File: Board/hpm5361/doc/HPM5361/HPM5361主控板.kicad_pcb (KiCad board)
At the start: 4 copper layers, 54.3 x 40 mm, 189 parts, among them J1 USB_C_Receptacle_USB2.0_16P, J2 Conn_02x05_Counter_Clockwise_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, J3 Conn_01x03_Pin, J4 Conn_01x02_Pin, J5 Conn_01x02_Pin, J7 Conn_01x02_Pin, Q1 AGM60P100A, Q2 PMBT3904, Q3 PMBT3904, Q4 AO3404A, U10 TJA1042TK-3, U11 TJA1042TK-3, U12 TJA1042TK-3, U13 RY8411, U14 LMR51450, U3 HPM5361ICB1, U5 USBLC6-2SC6, U6 W25Q128JVS, U7 SN65HVD75DRBR, U8 ICM-42688P-HXY, U9 TJA1042TK-3, Y1 24M

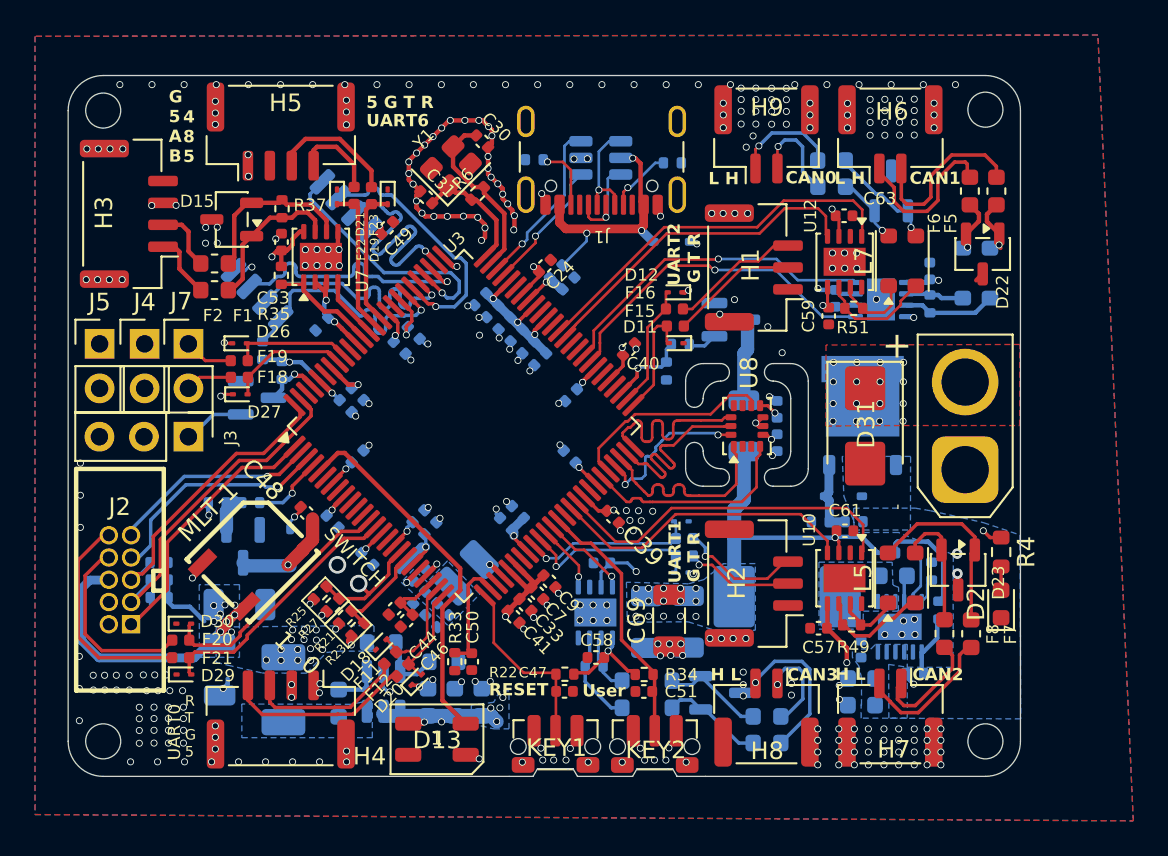
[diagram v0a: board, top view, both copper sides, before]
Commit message: 
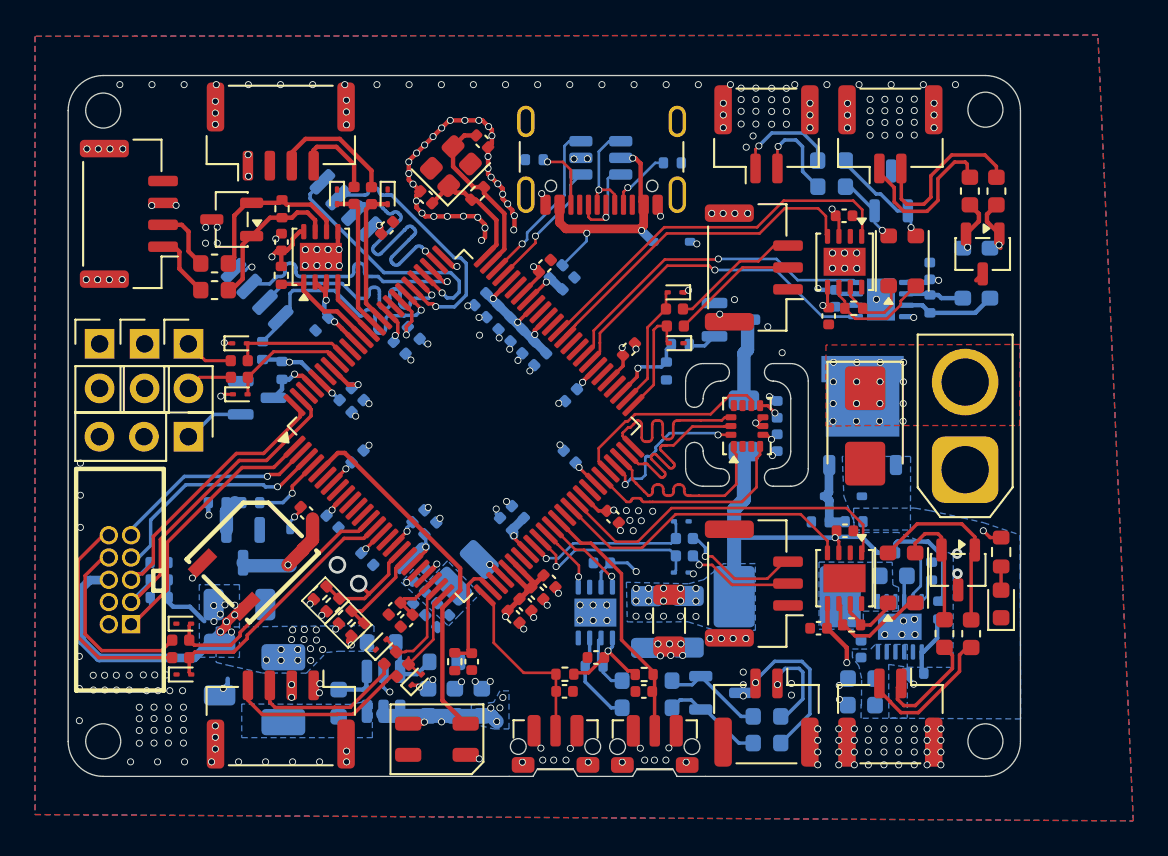
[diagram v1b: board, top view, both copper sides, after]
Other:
- board text removed: "0"
- board text removed: "1"
- board text removed: "4 8 5"
- board text removed: "5 G T R"
- board text removed: "CAN0"
- board text removed: "CAN1"
- board text removed: "CAN2"
- board text removed: "CAN3"
- board text removed: "G 5 A B"
- board text removed: "G T R"
- board text removed: "H L"
- board text removed: "L H"
- board text removed: "R T G 5"
- board text removed: "RESET"
- board text removed: "SWITCH"
- board text removed: "UART0"
- board text removed: "UART1"
- board text removed: "UART2"
- board text removed: "UART6"
- board text removed: "User"
